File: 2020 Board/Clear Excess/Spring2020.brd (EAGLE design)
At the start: 193.5 x 118.1 mm, 30 parts

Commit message: Some more cleanup
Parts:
- removed C1, C2, C4, C5: (no value), resistor:C025-025X050
- removed C22: (no value), resistor:C025-050X050
- removed LR2: ST26C32ABDR, BikeTeamLR:SOIC127P600X175-16N
- removed R4, R5, R7, R8: (no value), resistor:P0613/15
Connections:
- removed net 2AIN1: C4.1, LR2.1, R7.2, SV1.6
- removed net 2AIN2: C1.1, LR2.2, R4.1, SV1.5
- removed net 2AOUT: LR2.3
- removed net 2BIN1: C5.1, LR2.7, R8.2, SV1.4
- removed net 2BIN2: C2.1, LR2.6, R5.1, SV1.3
- removed net 2BOUT: LR2.5
- removed net N$2: C22.1
- removed net N$5: LR2.4
- net 3.3V: no longer C22.2, LR2.16, R4.2, R5.2, R7.1, R8.1
- net 5V: no longer SV1.2
- net GND: no longer C1.2, C2.2, C4.2, C5.2, LR2.14, LR2.15, LR2.8, SV1.1
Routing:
- net 3.3V: track 275.2 -> 34.6 mm, vias 23 -> 6
- net 2BOUT: track 163.4 -> 0.00 mm, vias 2 -> 0
- net 2AOUT: track 159.1 -> 0.00 mm, vias 2 -> 0
- net 2BIN1: track 129.3 -> 0.00 mm, vias 16 -> 0
- net 2AIN1: track 94.2 -> 0.00 mm, vias 10 -> 0
- net 2BIN2: track 90.0 -> 0.00 mm, vias 8 -> 0
- net 2AIN2: track 87.7 -> 0.00 mm, vias 10 -> 0
- net GND: track 63.5 -> 20.7 mm, vias 12 -> 4
- net N$2: track 10.2 -> 0.00 mm, vias 2 -> 0

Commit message: Final Cleaning of Bike
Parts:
- removed BIKEMOTOR, SERVO1, SERVO2: (no value), con-lstb:MA03-1
- removed C20: (no value), resistor:C025-050X050
- removed OP-AMP: OPAMP, Spring2016opamp:SOT95P280X145-5N
- removed SV1: (no value), con-lstb:MA03-2
- removed U$1: DUE(NORMAL), DUElib130425:DUE(NORMAL)
- added REAR-MOTOR: (no value), con-lstb:MA04-1
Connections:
- removed net 29: U$1.29
- removed net BAT+: SERVO1.2, SERVO2.2
- removed net BRAKE: RC.5, U$1.28
- removed net HORN: RC.1, U$1.32
- removed net LR-EN: U$1.26
- removed net N$3: BIKEMOTOR.2, OP-AMP.1, OP-AMP.4
- removed net N$4: BIKEMOTOR.1
- removed net PANIC: RC.2, U$1.27
- removed net REV: RC.3, U$1.33
- new net CH3: RC.3
- new net CH4: RC.4
- new net CH5: RC.5
- new net CH6: RC.6
- new net REVERSE: REAR-MOTOR.3
- net BGND: now also REAR-MOTOR.1; no longer C20.2, OP-AMP.2, SERVO1.3, SERVO2.3
- net CH1: now also RC.1; no longer RC.6, U$1.51
- net CH2: now also RC.2; no longer RC.4, U$1.25
- net FRONT-DIGI: no longer U$1.46
- net FRONT-PWM: no longer U$1.9
- net FRONT-PWMOUT/SERVO1: no longer SERVO1.1
- net GND: now also RC.7
- net MISO: no longer U$1.MISO_ICSP
- net MOSI: no longer U$1.MOSI_ICSP
- net REAR-PWM: no longer U$1.8
- net REAR-PWMOUT: now also REAR-MOTOR.2; no longer OP-AMP.3
- net REAR-PWMR/SERVO2: no longer SERVO2.1
- net REAR-TIMER: now also REAR-MOTOR.4; no longer BIKEMOTOR.3
- net REAR-TIMER-IN: no longer U$1.11
- net REG5V: no longer C20.1, OP-AMP.5
- net SCK: no longer U$1.SCK_ICSP
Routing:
- net CH1: track 247.6 -> 0.00 mm, vias 8 -> 0
- net CH6: track 0.00 -> 245.8 mm, vias 0 -> 8
- net CH4: track 0.00 -> 216.8 mm
- net REV: track 215.8 -> 0.00 mm, vias 6 -> 0
- net CH3: track 0.00 -> 214.0 mm, vias 0 -> 6
- net PANIC: track 200.7 -> 0.00 mm
- net BRAKE: track 200.5 -> 0.00 mm, vias 4 -> 0
- net CH5: track 0.00 -> 198.7 mm, vias 0 -> 4
- net 29: track 169.5 -> 0.00 mm, vias 24 -> 0
- net REAR-TIMER: track 218.2 -> 99.3 mm
- net BAT+: track 70.4 -> 0.00 mm
- net LR-EN: track 50.5 -> 0.00 mm, vias 6 -> 0
- net MISO: track 50.6 -> 10.7 mm, vias 6 -> 2
- net HORN: track 32.9 -> 0.00 mm, vias 6 -> 0
- net CH2: track 218.6 -> 199.5 mm
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
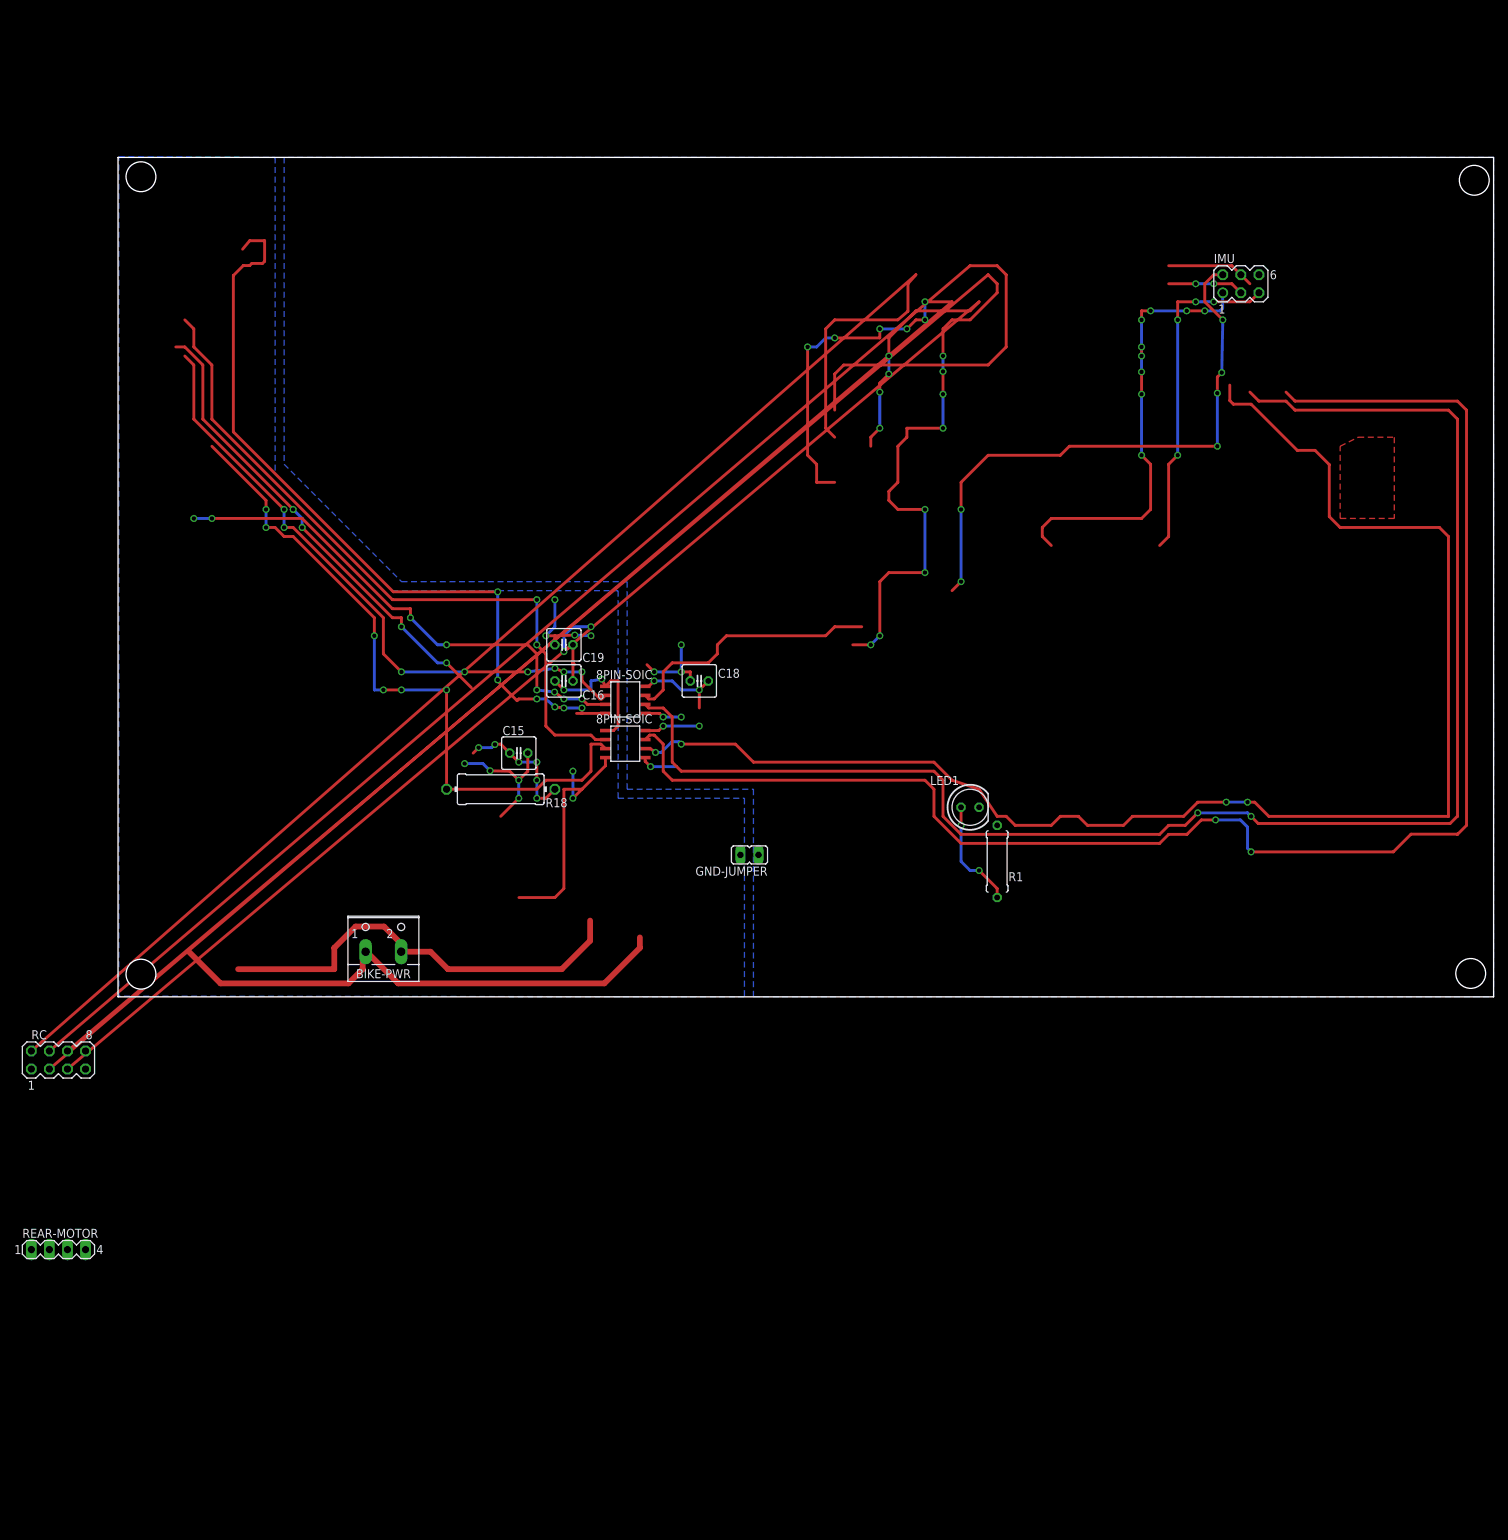
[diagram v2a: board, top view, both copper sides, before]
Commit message: MCR
Added the front motor controller, once clarification comes in on the isolator, can deal with the isolator connection as well
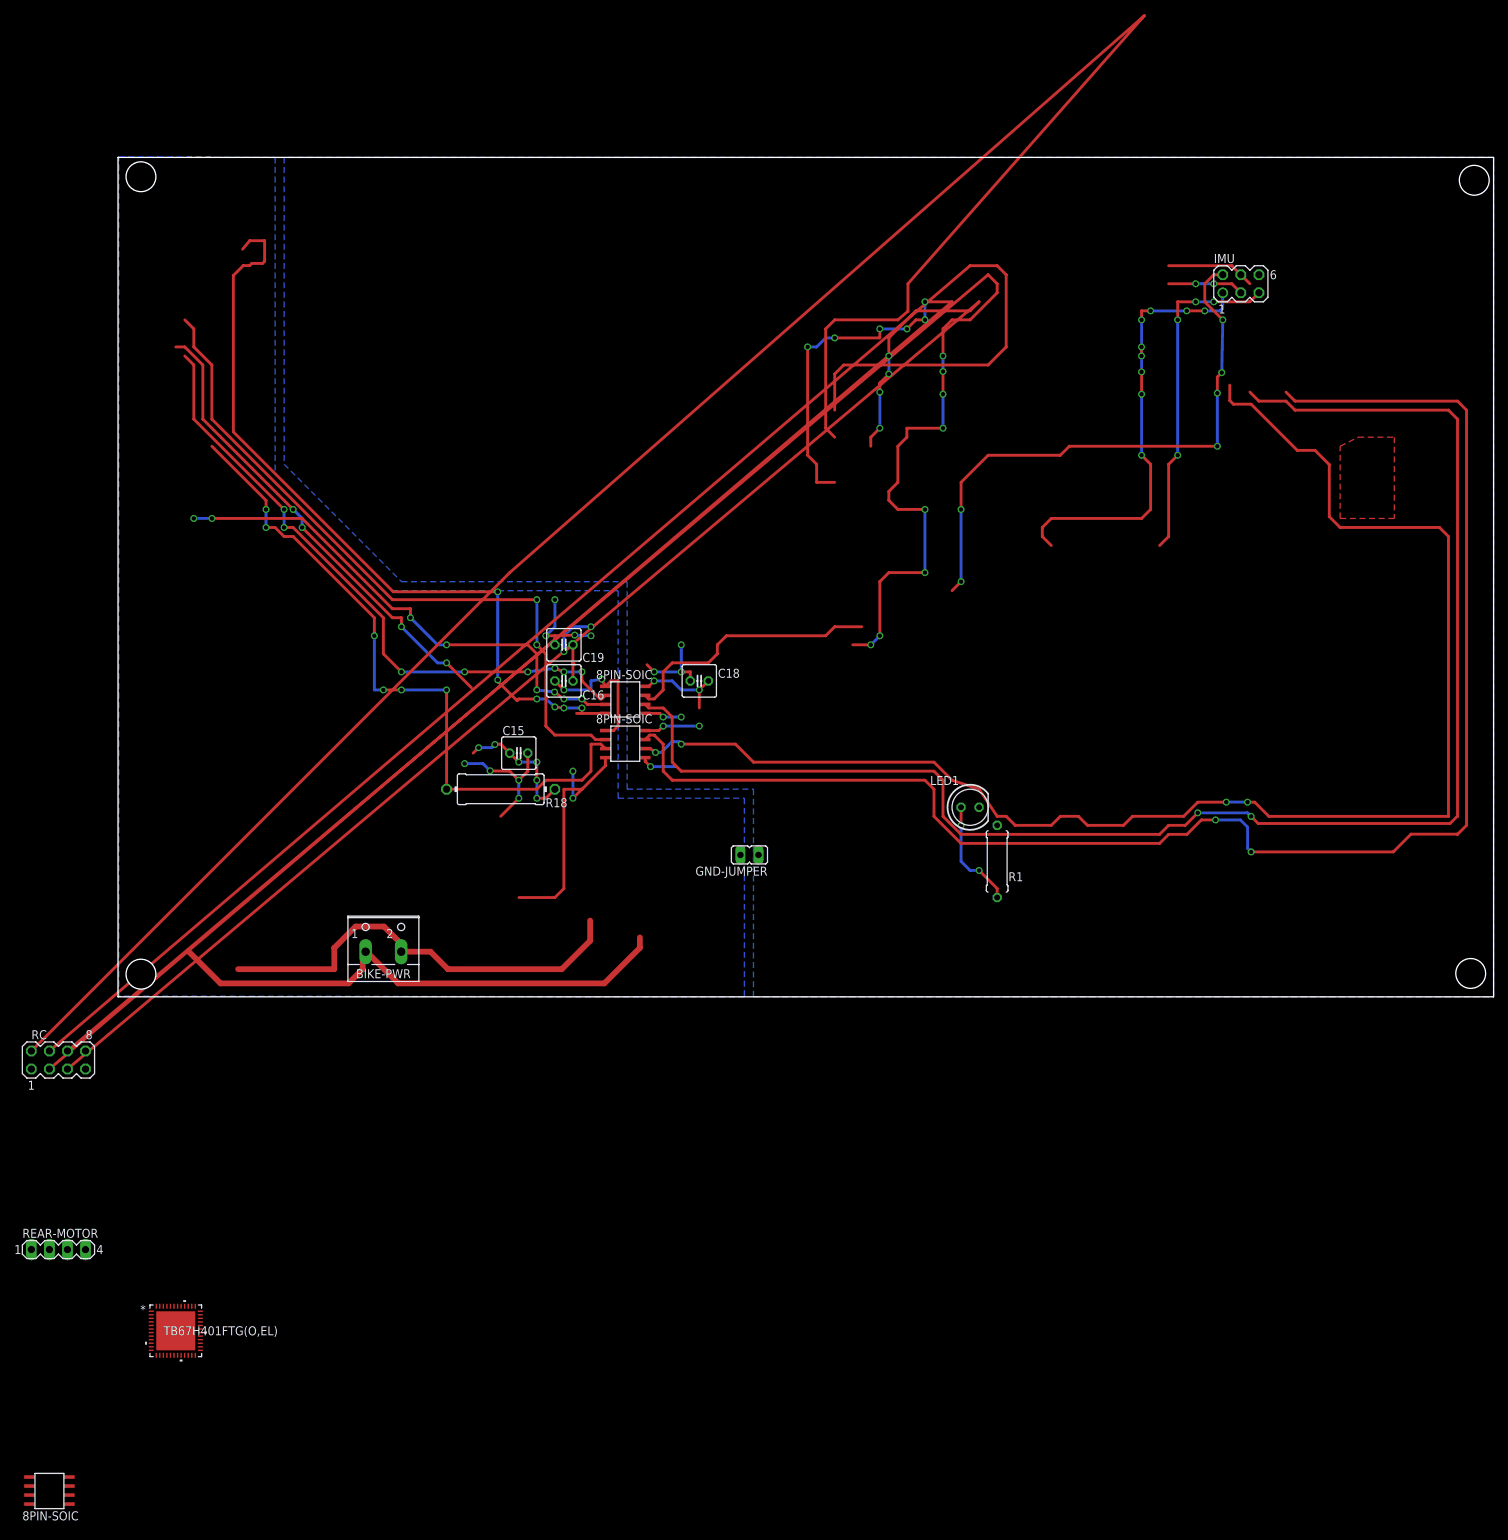
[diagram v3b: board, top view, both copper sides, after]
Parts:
- added U$1: IL-711, Spring2016Optoisolator:8PINSOIC
- added U1: TB67H401FTG(O,EL), mclr:P-VQFN48-0707-0P50-004_TOS
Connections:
- new net GND1: U$1.4
- new net GND2: U$1.5
- new net I_1: U1.2, U1.44
- new net I_2: U1.3, U1.45
- new net VCC: U1.34, U1.46, U1.47
- new net VDD1: U$1.1
- new net VDD2: U$1.8
- new net VREFA: U1.42
- new net VREFB: U1.41
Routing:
- net CH2: track 199.5 -> 296.5 mm
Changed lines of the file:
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@@
 <layer number="54" name="bGND_GNDA" color="1" fill="9" visible="no" active="no"/>
 <layer number="56" name="wert" color="7" fill="1" visible="no" active="no"/>
+<layer number="88" name="SimResults" color="9" fill="1" visible="no" active="no"/>
+<layer number="89" name="SimProbes" color="9" fill="1" visible="no" active="no"/>
 <layer number="90" name="Modules" color="5" fill="1" visible="no" active="no"/>
 <layer number="91" name="Nets" color="2" fill="1" visible="no" active="no"/>
@@
 <attribute name="VALUE" x="95.96" y="14.001" size="1.27" layer="27" ratio="10" rot="R180"/>
 </element>
+<element name="U1" library="mclr" package="P-VQFN48-0707-0P50-004_TOS" value="TB67H401FTG(O,EL)" x="12.7" y="-55.88" smashed="yes">
+<attribute name="COPYRIGHT" value="Copyright (C) 2022 Ultra Librarian. All rights reserved." x="12.7" y="-55.88" size="1.778" layer="27" display="off"/>
+<attribute name="DIGI-KEY_PART_NUMBER_1" value="TB67H401FTG(OEL)TR-ND" x="12.7" y="-55.88" size="1.778" layer="27" display="off"/>
+<attribute name="DIGI-KEY_PART_NUMBER_2" value="TB67H401FTG(OEL)CT-ND" x="12.7" y="-55.88" size="1.778" layer="27" display="off"/>
+<attribute name="DIGI-KEY_PART_NUMBER_3" value="TB67H401FTG(OEL)DKR-ND" x="12.7" y="-55.88" size="1.778" layer="27" display="off"/>
+<attribute name="MANUFACTURER_PART_NUMBER" value="TB67H401FTG(O,EL)" x="12.7" y="-55.88" size="1.778" layer="27" display="off"/>
+<attribute name="MFR_NAME" value="Toshiba Electronic Devices &amp; Storage Co." x="12.7" y="-55.88" size="1.778" layer="27" display="off"/>
+<attribute name="NAME" x="9.4234" y="-56.515" size="1.27" layer="27" ratio="6" rot="SR0"/>
+<attribute name="VALUE" x="10.9728" y="-56.515" size="1.27" layer="21" ratio="6" rot="SR0"/>
+</element>
+<element name="U$1" library="Spring2016Optoisolator" package="8PINSOIC" value="IL-711" x="-5.08" y="-78.74" smashed="yes"/>
 </elements>
 <signals>
@@
 <wire x1="114.3" y1="86.36" x2="115.72" y2="87.58" width="0.4064" layer="1"/>
 <wire x1="115.72" y1="87.58" x2="115.72" y2="91.44" width="0.4064" layer="1"/>
-<wire x1="115.72" y1="91.44" x2="116.84" y2="92.71" width="0.4064" layer="1"/>
-<wire x1="116.84" y1="92.71" x2="-7.62" y2="-16.51" width="0.4064" layer="1"/>
+<wire x1="115.72" y1="91.44" x2="148.988059375" y2="129.163603125" width="0.4064" layer="1"/>
+<wire x1="148.988059375" y1="129.163603125" x2="59.69" y2="50.8" width="0.4064" layer="1"/>
+<wire x1="59.69" y1="50.8" x2="-7.62" y2="-16.51" width="0.4064" layer="1"/>
 </signal>
 <signal name="CH3">
@@
 <wire x1="127" y1="92.71" x2="-2.54" y2="-16.51" width="0.4064" layer="1"/>
 </signal>
+<signal name="VCC">
+<contactref element="U1" pad="34"/>
+<contactref element="U1" pad="46"/>
+<contactref element="U1" pad="47"/>
+<wire x1="10.45" y1="-52.4276" x2="10.95" y2="-52.4276" width="0" layer="19" extent="1-1"/>
+<wire x1="16.1524" y1="-54.13" x2="10.95" y2="-52.4276" width="0" layer="19" extent="1-1"/>
+</signal>
+<signal name="VREFB">
+<contactref element="U1" pad="41"/>
+</signal>
+<signal name="VREFA">
+<contactref element="U1" pad="42"/>
+</signal>
+<signal name="I_1">
+<contactref element="U1" pad="2"/>
+<contactref element="U1" pad="44"/>
+<wire x1="11.95" y1="-52.4276" x2="9.2476" y2="-53.63" width="0" layer="19" extent="1-1"/>
+</signal>
+<signal name="I_2">
+<contactref element="U1" pad="45"/>
+<contactref element="U1" pad="3"/>
+<wire x1="11.45" y1="-52.4276" x2="9.2476" y2="-54.13" width="0" layer="19" extent="1-1"/>
+</signal>
+<signal name="VDD1">
+<contactref element="U$1" pad="1"/>
+</signal>
+<signal name="GND1">
+<contactref element="U$1" pad="4"/>
+</signal>
+<signal name="GND2">
+<contactref element="U$1" pad="5"/>
+</signal>
+<signal name="VDD2">
+<contactref element="U$1" pad="8"/>
+</signal>
 </signals>
